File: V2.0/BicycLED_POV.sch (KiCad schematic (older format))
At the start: 57 parts, among them IC1 AT45DBXX1, IC2 AT91SAM7S512/256/128/64/321-AU, P1 CONN_2, Q1 BSH207, Q2 BSH207, Q3 2N2002K, SW1 bootloader, U1 CONN_MICROSD, U2 MCP73811/2, U3 CONN_JTAG_ARM, U4 USBCONN, U5 AH173, U6 FAN2502-XX, X1 18.432 MHz

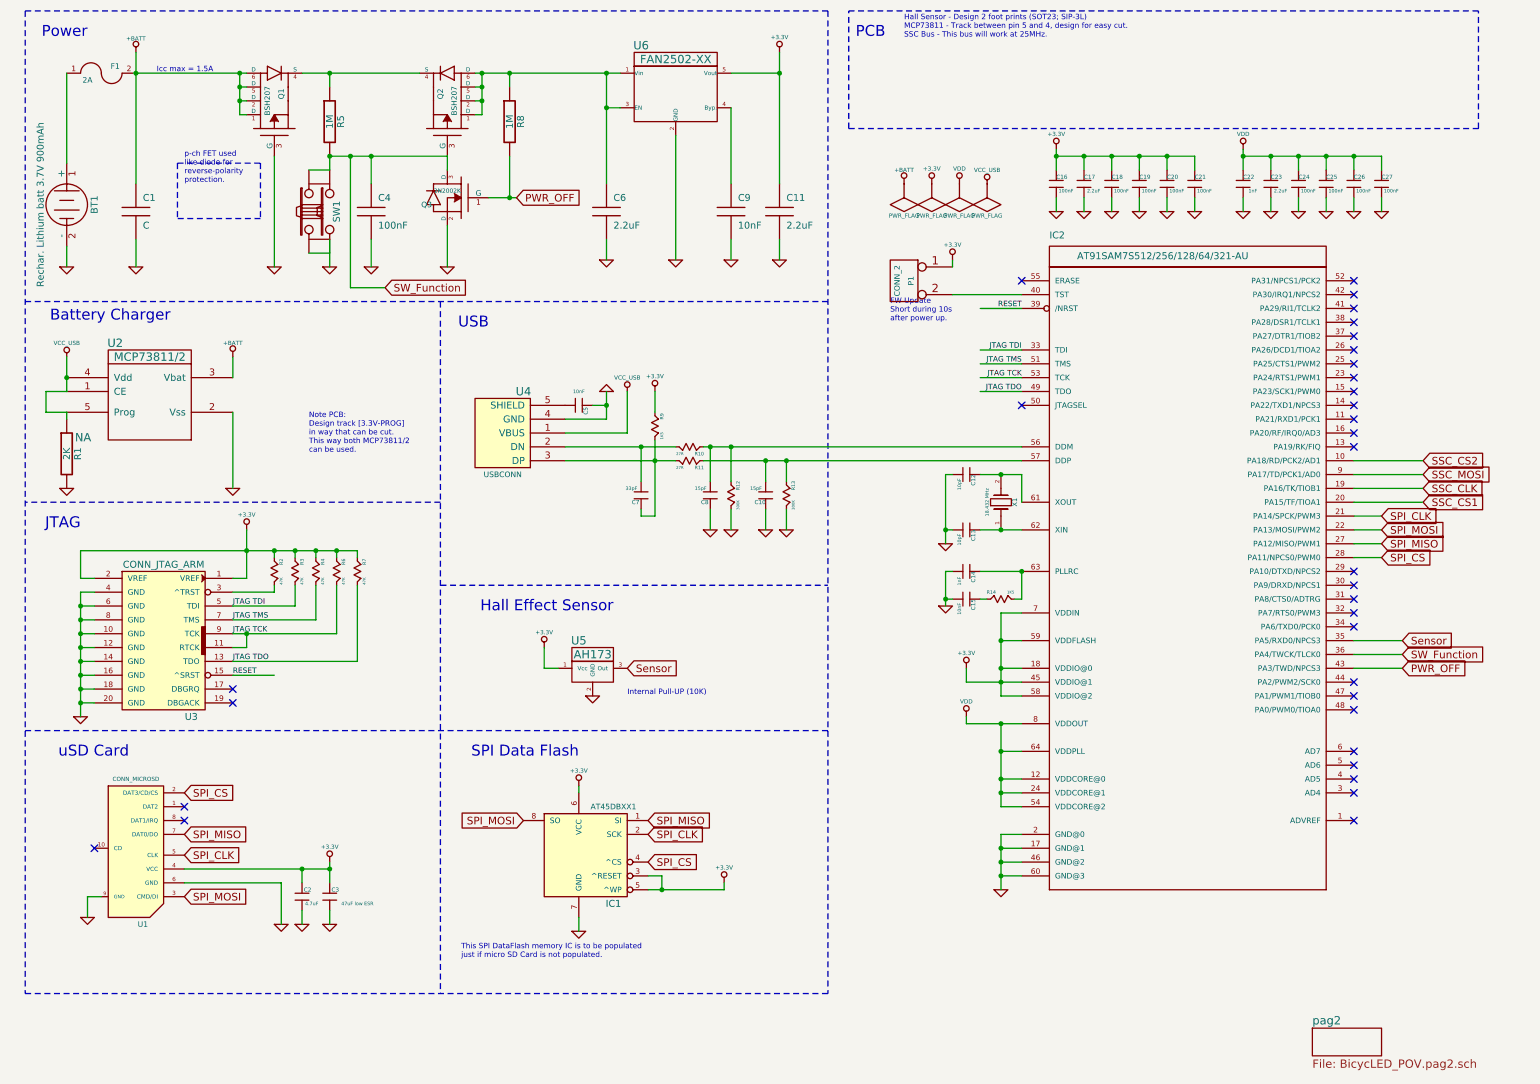
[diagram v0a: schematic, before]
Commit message: Alteração Esquemático. Criado PCB
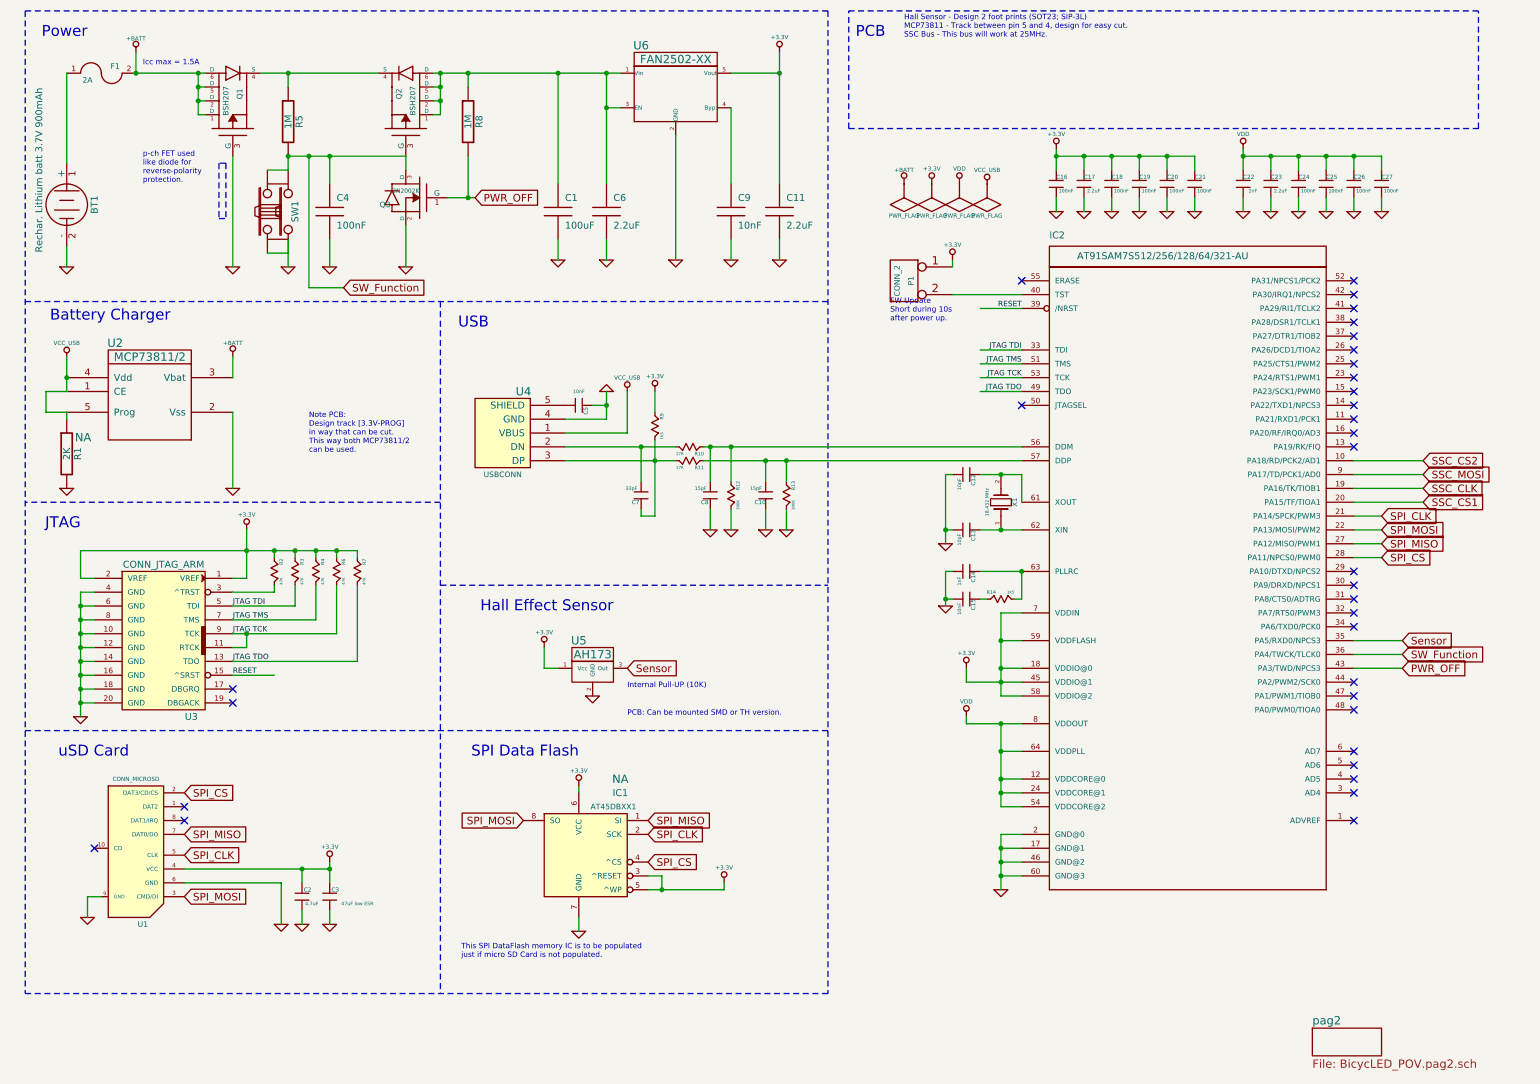
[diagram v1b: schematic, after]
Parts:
- C1: value C -> 100uF
- IC1: Populate (none) -> NA
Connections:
- wire segments 196 -> 197
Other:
- note added: "PCB: Can be mounted SMD or TH version."
- moved on the sheet: C1, C4, Q1, Q2, Q3, R5, R8, SW1

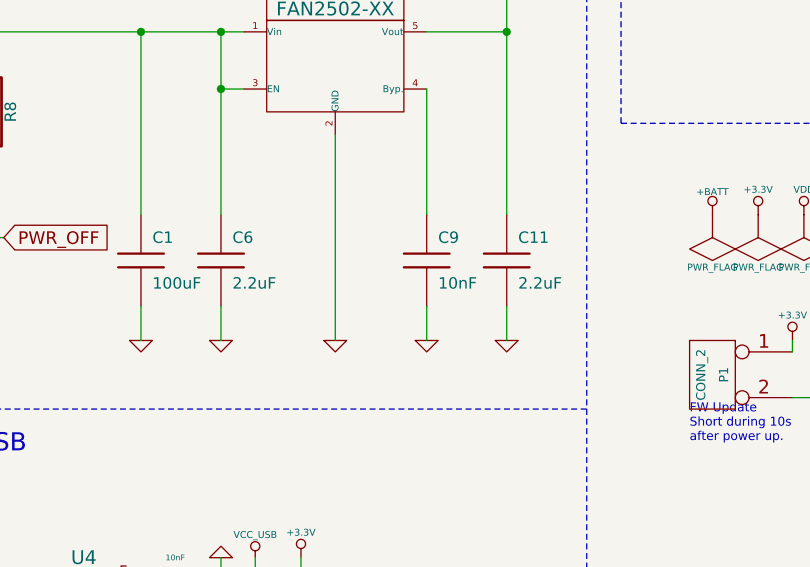
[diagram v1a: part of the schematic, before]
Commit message: 2.2uF cap change to 4.7uF
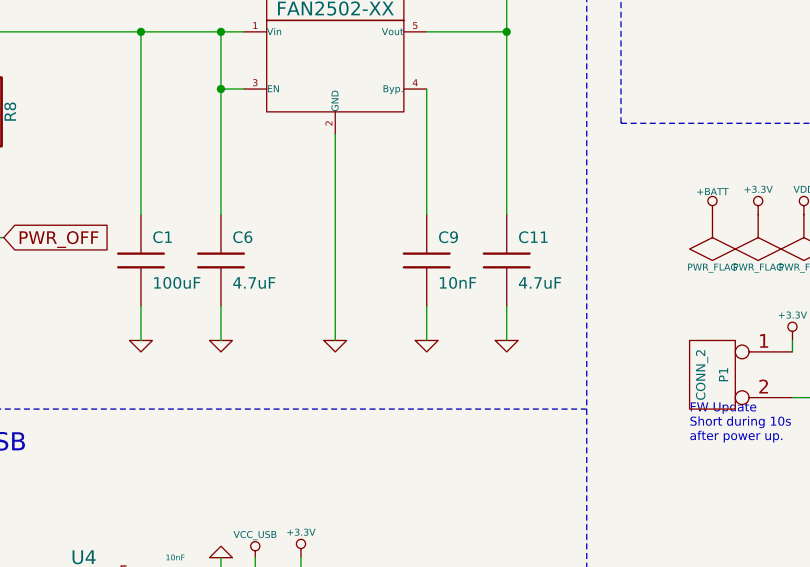
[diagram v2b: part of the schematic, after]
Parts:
- C11, C6: value 2.2uF -> 4.7uF
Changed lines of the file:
@@
-EESchema Schematic File Version 2  date 11/05/2010 05:53:48
+EESchema Schematic File Version 2  date 12/05/2010 01:20:40
 LIBS:regul
 LIBS:switch_FSM2JSMA
@@
 Sheet 1 2
 Title "BicycLED POV"
-Date "11 may 2010"
+Date "12 may 2010"
 Rev "v 2.0"
 Comp "Hardware BOX"
@@
 P 4750 2050
 F 0 "C6" H 4800 2150 50  0000 L CNN
-F 1 "2.2uF" H 4800 1950 50  0000 L CNN
+F 1 "4.7uF" H 4800 1950 50  0000 L CNN
 F 4 "" H 4750 2050 60  0001 C CNN "Campo1"
 F 5 "" H 4750 2050 60  0001 C CNN "Campo2"
@@
 P 6000 2050
 F 0 "C11" H 6050 2150 50  0000 L CNN
-F 1 "2.2uF" H 6050 1950 50  0000 L CNN
+F 1 "4.7uF" H 6050 1950 50  0000 L CNN
 F 4 "" H 6000 2050 60  0001 C CNN "Campo1"
 F 5 "" H 6000 2050 60  0001 C CNN "Campo2"

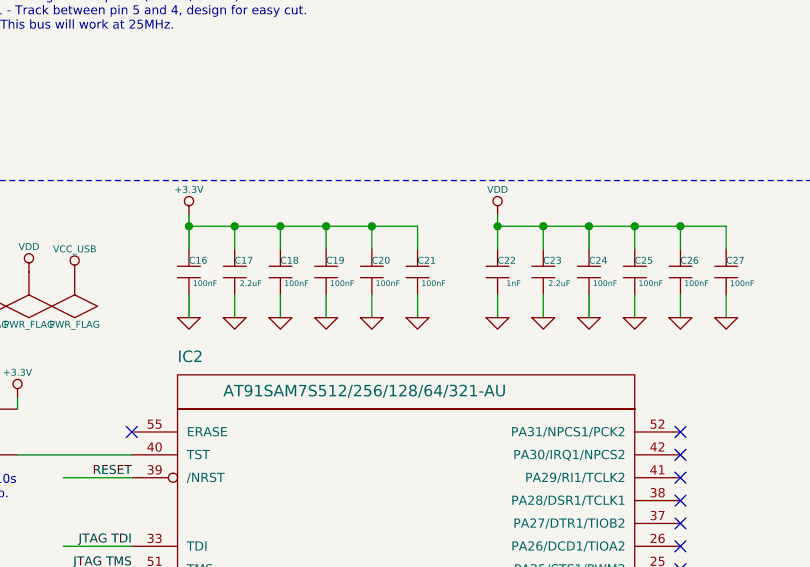
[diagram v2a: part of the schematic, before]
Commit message: Net List: edited. Sch: Cap 2.2uF changed to 4.7uF
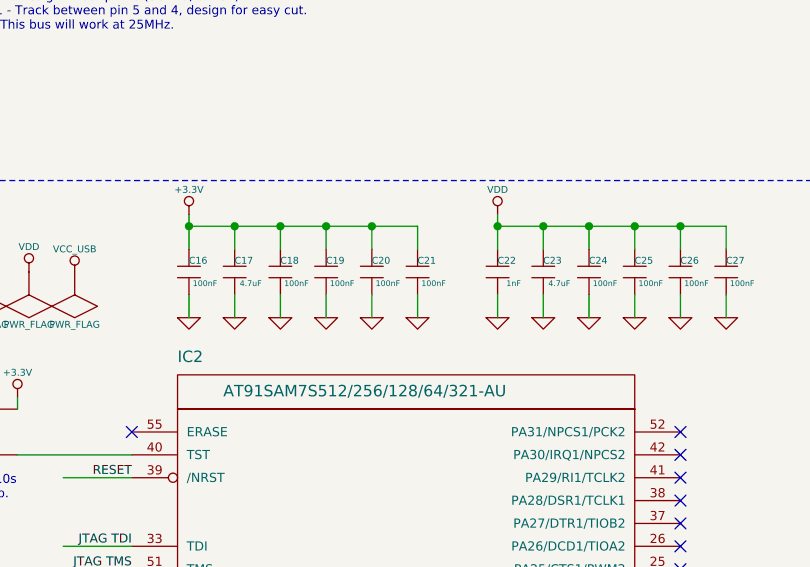
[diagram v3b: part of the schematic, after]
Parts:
- C17, C23: value 2.2uF -> 4.7uF
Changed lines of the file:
@@
-EESchema Schematic File Version 2  date 12/05/2010 01:20:40
+EESchema Schematic File Version 2  date 12/05/2010 02:02:46
 LIBS:regul
 LIBS:switch_FSM2JSMA
@@
 P 9550 1850
 F 0 "C23" V 9500 1890 30  0000 C CNN
-F 1 "2.2uF" V 9600 1920 25  0000 C CNN
+F 1 "4.7uF" V 9600 1920 25  0000 C CNN
 F 4 "" H 9550 1850 60  0001 C CNN "Campo1"
 F 5 "" H 9550 1850 60  0001 C CNN "Campo2"
@@
 P 8200 1850
 F 0 "C17" V 8150 1890 30  0000 C CNN
-F 1 "2.2uF" V 8250 1920 25  0000 C CNN
+F 1 "4.7uF" V 8250 1920 25  0000 C CNN
 F 4 "" H 8200 1850 60  0001 C CNN "Campo1"
 F 5 "" H 8200 1850 60  0001 C CNN "Campo2"

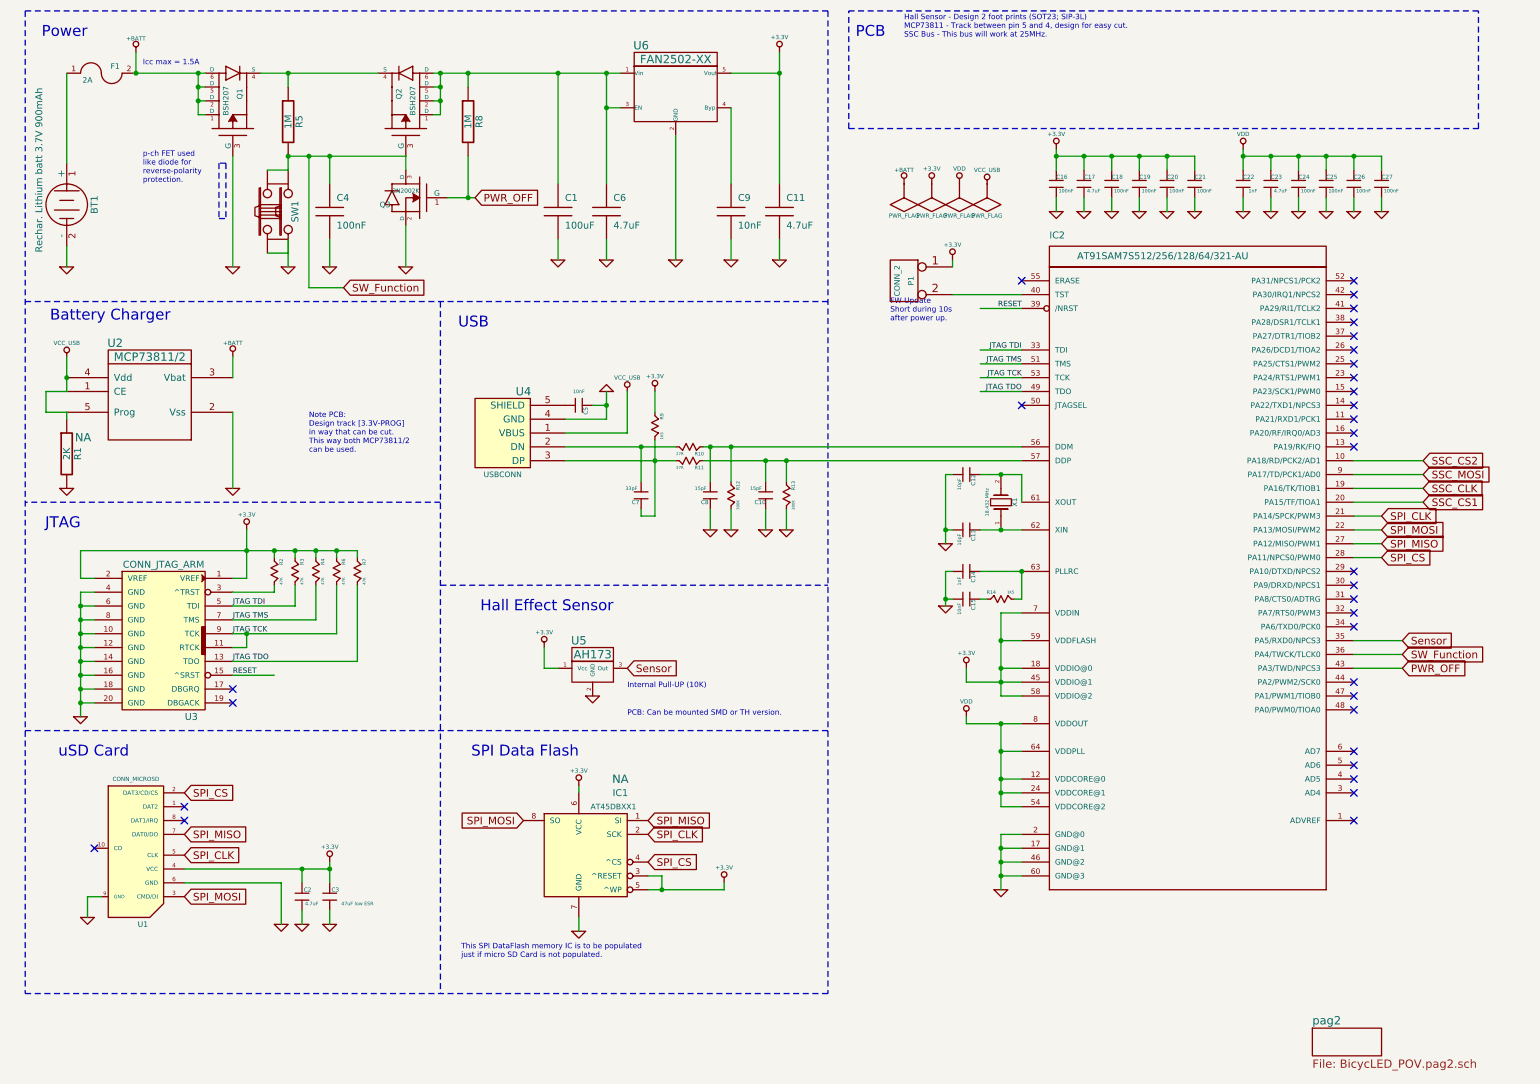
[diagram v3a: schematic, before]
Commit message: Actualizei as etiquetas do JTAG para globais, de modo a ficarem todas a ser do mesmo tipo no esquema.
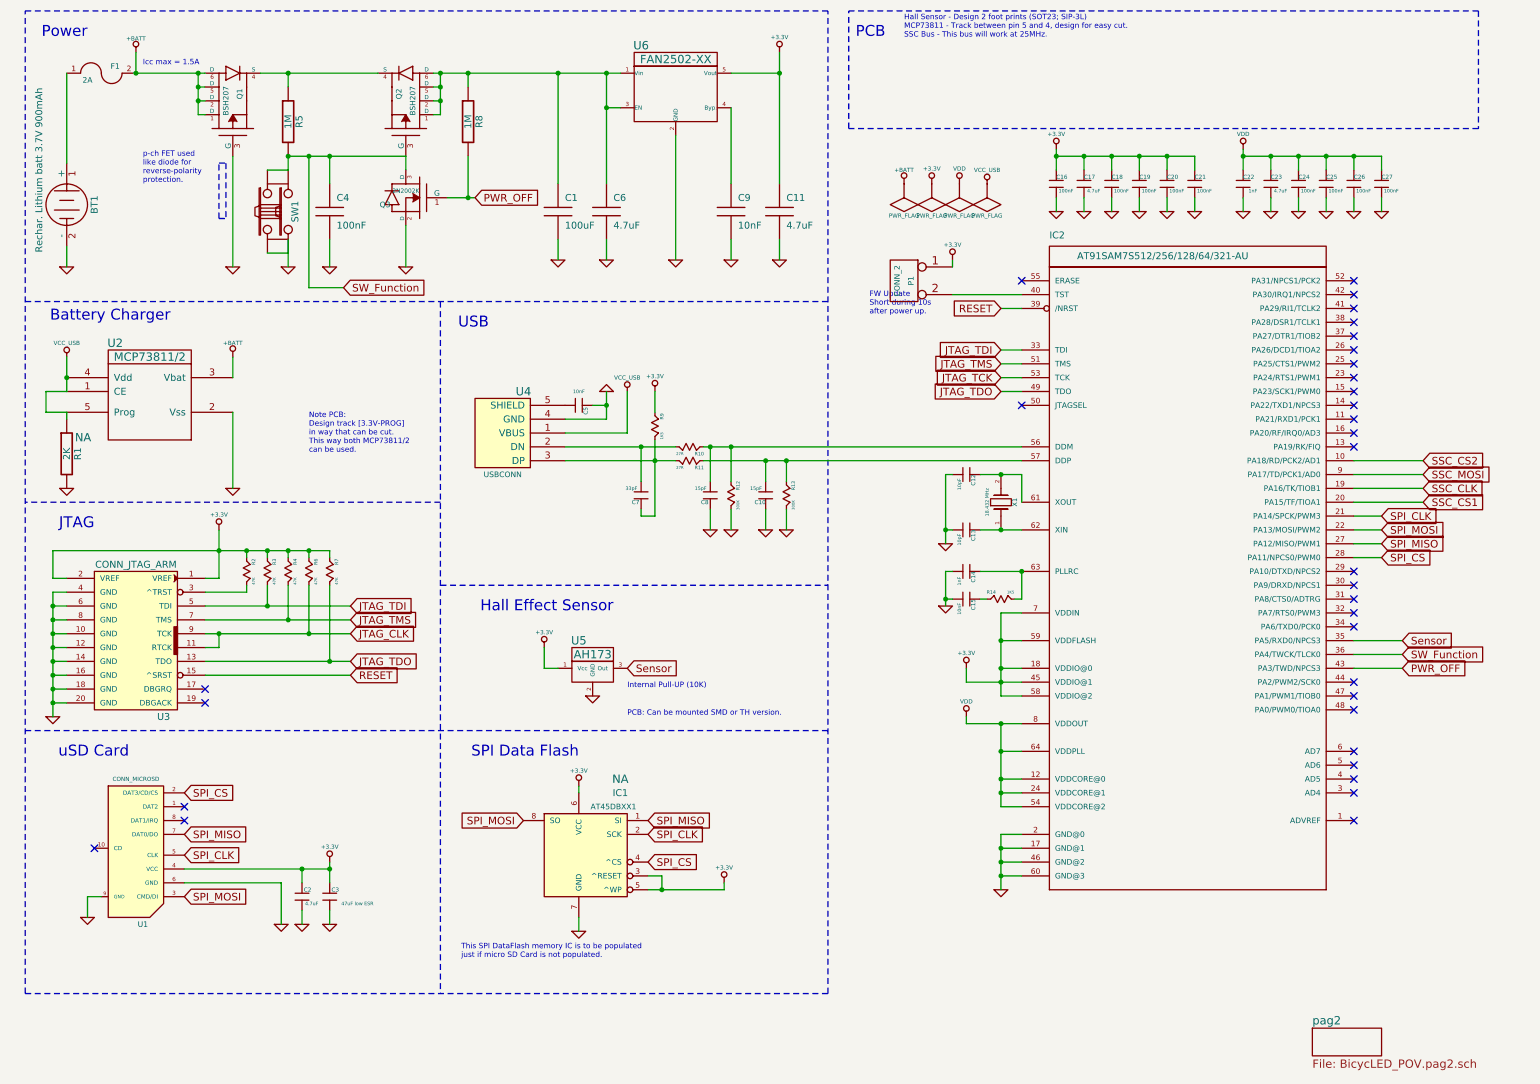
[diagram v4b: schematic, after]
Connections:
- net labels added: JTAG_CLK, JTAG_TCK, JTAG_TDI, JTAG_TDO, JTAG_TMS
- net labels removed: JTAG TCK, JTAG TDI, JTAG TDO, JTAG TMS
- wire segments 197 -> 268
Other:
- moved on the sheet: R2, R3, R4, R6, R7, U3

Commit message: brd: created
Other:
- moved on the sheet: C10, C12, C13, C14, C15, C16, C17, C18, C19, C20, C21, C22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
